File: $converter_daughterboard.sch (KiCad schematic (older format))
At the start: 45 parts, among them P1 IN+, P10 SC-, P2 IN GND, P3 OUT+, P4 OUT GND, P5 PC, P6 PR, P7 SC+, P8 IC_POW-, P9 IC_POW+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

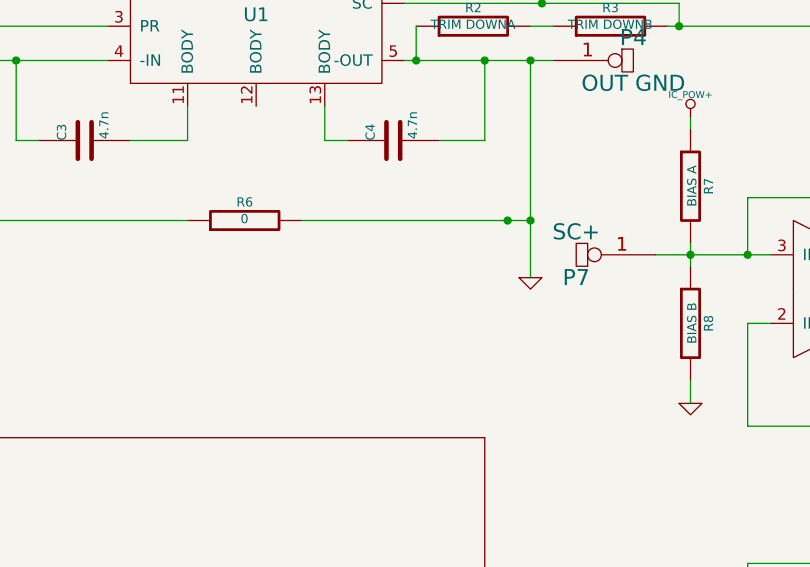
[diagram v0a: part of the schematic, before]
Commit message: added protection circuitry to converter daughterboard. should be ready for fabrication
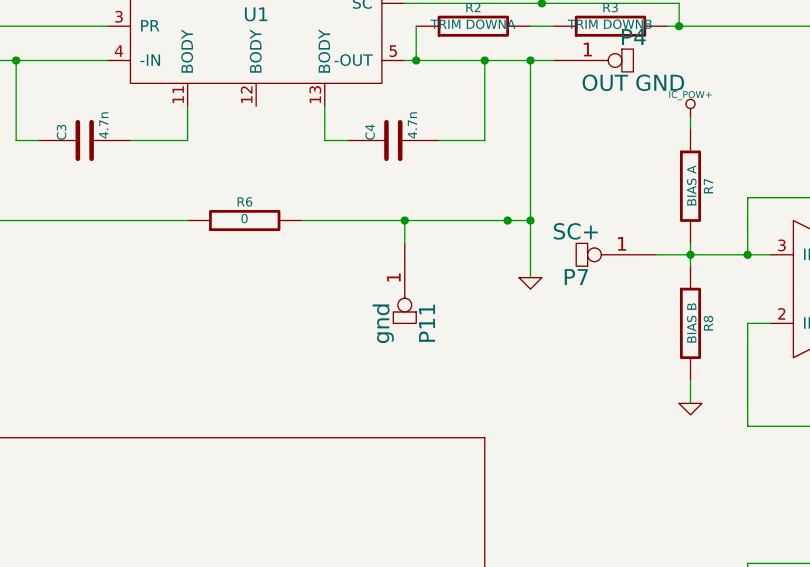
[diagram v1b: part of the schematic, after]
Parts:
- added P11: gnd, ~, symbol CONNECTOR
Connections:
- net GND: now also P11.1 (W)
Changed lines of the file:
@@
 Wire Wire Line
 	7350 2400 7350 2350
+$Comp
+L CONNECTOR P11
+U 1 1 56EE5605
+P 6100 2900
+F 0 "P11" H 6450 3000 70  0000 C CNN
+F 1 "gnd" H 6450 2800 70  0000 C CNN
+F 2 "~" H 6100 2900 60  0000 C CNN
+F 3 "~" H 6100 2900 60  0000 C CNN
+	1    6100 2900
+	0    1    1    0
+$EndComp
+Wire Wire Line
+	6100 2900 6100 2800
+Connection ~ 6100 2800
 $EndSCHEMATC

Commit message: updated converter board and created fab files
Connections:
- net GNDA: now also C6.2
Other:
- moved on the sheet: C6
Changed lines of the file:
@@
 Sheet 1 1
 Title "noname.sch"
-Date "20 mar 2016"
+Date "25 mar 2016"
 Rev ""
 Comp ""
@@
 L C C6
 U 1 1 568A29C9
-P 3950 1900
-F 0 "C6" H 3950 2000 40  0000 L CNN
-F 1 ".1u" H 3956 1815 40  0000 L CNN
-F 2 "~" H 3988 1750 30  0000 C CNN
-F 3 "~" H 3950 1900 60  0000 C CNN
-	1    3950 1900
+P 3950 1850
+F 0 "C6" H 3950 1950 40  0000 L CNN
+F 1 ".1u" H 3956 1765 40  0000 L CNN
+F 2 "~" H 3988 1700 30  0000 C CNN
+F 3 "~" H 3950 1850 60  0000 C CNN
+	1    3950 1850
 	1    0    0    -1
 $EndComp
@@
 	6100 2900 6100 2800
 Connection ~ 6100 2800
+Wire Wire Line
+	3950 2050 3950 2100
+Connection ~ 3950 2100
 $EndSCHEMATC

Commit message: revised converter daughterboard to adjust setpoint signal to account for current dropped across low side sense resistor
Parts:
- removed P10: SC-, ~, symbol CONNECTOR
- added R19, R20: R, ~, symbol R
- added unit 4 of U3
- P11: value gnd -> SC-
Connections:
- net GND: now also R19.2; no longer P11.1 (W)
- net IC_POW+: now also U3.4 (IC_POW+)
- net IC_POW-: now also U3.13 (IC_POW-)
- net at U3.5 (IN+): now also R20.1, U3.16 (OUT)
- new net: P11.1 (W), U3.14 (IN+)
- new net: R19.1, R20.2, U3.15 (IN-)
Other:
- moved on the sheet: P11, U2
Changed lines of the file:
@@
 Sheet 1 1
 Title "noname.sch"
-Date "25 mar 2016"
+Date "13 apr 2016"
 Rev ""
 Comp ""
@@
 L DAUGHTERBOARD_MOUNT U2
 U 1 1 538CD3F3
-P 5300 4450
-F 0 "U2" H 5300 4350 60  0000 C CNN
-F 1 "DAUGHTERBOARD_MOUNT" H 5300 4450 60  0000 C CNN
-F 2 "" H 5300 4450 60  0000 C CNN
-F 3 "" H 5300 4450 60  0000 C CNN
-	1    5300 4450
+P 1950 3300
+F 0 "U2" H 1950 3200 60  0000 C CNN
+F 1 "DAUGHTERBOARD_MOUNT" H 1950 3300 60  0000 C CNN
+F 2 "" H 1950 3300 60  0000 C CNN
+F 3 "" H 1950 3300 60  0000 C CNN
+	1    1950 3300
 	1    0    0    -1
 $EndComp
@@
 $EndComp
 Wire Wire Line
-	3950 1700 3950 1650
+	3950 1450 3950 1700
 Connection ~ 3950 1650
 $Comp
@@
 	1    0    0    -1
 $EndComp
-$Comp
-L CONNECTOR P10
-U 1 1 56ECD126
-P 7250 5050
-F 0 "P10" H 7600 5150 70  0000 C CNN
-F 1 "SC-" H 7600 4950 70  0000 C CNN
-F 2 "~" H 7250 5050 60  0000 C CNN
-F 3 "~" H 7250 5050 60  0000 C CNN
-	1    7250 5050
-	-1   0    0    1
-$EndComp
-Wire Wire Line
-	7250 5050 7700 5050
+Wire Wire Line
+	6950 5050 7700 5050
 $Comp
 L R R18
@@
 L CONNECTOR P11
 U 1 1 56EE5605
-P 6100 2900
-F 0 "P11" H 6450 3000 70  0000 C CNN
-F 1 "gnd" H 6450 2800 70  0000 C CNN
-F 2 "~" H 6100 2900 60  0000 C CNN
-F 3 "~" H 6100 2900 60  0000 C CNN
-	1    6100 2900
+P 5950 5400
+F 0 "P11" H 6300 5500 70  0000 C CNN
+F 1 "SC-" H 6300 5300 70  0000 C CNN
+F 2 "~" H 5950 5400 60  0000 C CNN
+F 3 "~" H 5950 5400 60  0000 C CNN
+	1    5950 5400
 	0    1    1    0
 $EndComp
-Wire Wire Line
-	6100 2900 6100 2800
-Connection ~ 6100 2800
 Wire Wire Line
 	3950 2050 3950 2100
 Connection ~ 3950 2100
+$Comp
+L LT1014 U3
+U 4 1 570DDFEC
+P 6550 5050
+F 0 "U3" H 6550 4700 60  0000 C CNN
+F 1 "LT1014" H 6550 4600 60  0000 C CNN
+F 2 "~" H 6550 5050 60  0000 C CNN
+F 3 "~" H 6550 5050 60  0000 C CNN
+	4    6550 5050
+	1    0    0    1
+$EndComp
+$Comp
+L R R20
+U 1 1 570DE1ED
+P 6650 4400
+F 0 "R20" V 6730 4400 40  0000 C CNN
+F 1 "R" V 6657 4401 40  0000 C CNN
+F 2 "~" V 6580 4400 30  0000 C CNN
+F 3 "~" H 6650 4400 30  0000 C CNN
+	1    6650 4400
+	0    1    1    0
+$EndComp
+$Comp
+L R R19
+U 1 1 570DE1F3
+P 5750 4900
+F 0 "R19" V 5830 4900 40  0000 C CNN
+F 1 "R" V 5757 4901 40  0000 C CNN
+F 2 "~" V 5680 4900 30  0000 C CNN
+F 3 "~" H 5750 4900 30  0000 C CNN
+	1    5750 4900
+	0    1    1    0
+$EndComp
+Wire Wire Line
+	5950 5400 5950 5200
+Wire Wire Line
+	5950 5200 6150 5200
+Wire Wire Line
+	6000 4900 6150 4900
+Wire Wire Line
+	6100 4900 6100 4400
+Wire Wire Line
+	6100 4400 6400 4400
+Connection ~ 6100 4900
+Wire Wire Line
+	6900 4400 7250 4400
+Wire Wire Line
+	7250 4400 7250 5050
+Connection ~ 7250 5050
+Wire Wire Line
+	5500 4900 5500 3100
+Wire Wire Line
+	5500 3100 6250 3100
+Wire Wire Line
+	6250 3100 6250 2800
+Connection ~ 6250 2800
+Wire Wire Line
+	7850 1400 7850 1650
+Connection ~ 7850 1650
 $EndSCHEMATC
